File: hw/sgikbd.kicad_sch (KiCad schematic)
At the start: 16 parts, among them CON1 ISP, J1 SERIAL, SW1 RESET, SW2 SW_DPDT_x2, U1 ATMEGA88-20PU, U2 intkbd, U3 ps2conn, U4 kbout, Y1 Crystal

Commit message: schematic progress
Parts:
- removed CON1: ISP, AVR-ISP-6, symbol sgikbd-rescue:AVR-ISP-6
- removed J1: SERIAL, symbol sgikbd-rescue:CONN_01X04
- removed R2, R3: 4.7k, symbol sgikbd-rescue:R
- removed SW2: SW_DPDT_x2, symbol sgikbd-rescue:SW_DPDT_x2
- removed U1: ATMEGA88-20PU, DIL28, symbol sgikbd-rescue:ATMEGA88-20PU
- removed U2: intkbd, symbol sgikbd-rescue:sgikbd_conn
- removed U3: ps2conn, symbol sgikbd-rescue:ps2conn
- removed U4: kbout, symbol sgikbd-rescue:sgikbd_conn
- added C? (x4): 0.33uF, symbol Device:C_Polarized
- added J?: AVR-ISP, symbol Connector:AVR-ISP-6
- added R? (x2): 4.7k, symbol sgikbd-rescue:R
- added U?: sgi-db15, Connector_Dsub:DSUB-15_Female_Horizontal_P2.77x2.84mm_EdgePinOffset7.70mm_Housed_MountingHolesOffset9.12mm, symbol sgikbd:sgi-db15
- added U? (x3): LM358, symbol Amplifier_Operational:LM358
- added U?: ps2kbd, symbol sgikbd:ps2conn
- added U?: sgi-db9, Connector_Dsub:DSUB-9_Female_Horizontal_P2.77x2.84mm_EdgePinOffset7.70mm_Housed_MountingHolesOffset9.12mm, symbol sgikbd:sgi-db9
- added U?: L7805, symbol Regulator_Linear:L7805
- added U?: L7905, symbol Regulator_Linear:L7905
- added U?: ps2mouse, symbol sgikbd:ps2conn
- added U?: ATmega328PB-A, Package_QFP:TQFP-32_7x7mm_P0.8mm, symbol MCU_Microchip_ATmega:ATmega328PB-A
- added U?: sgi-mdin6, symbol sgikbd:sgi-mdin6
- Y1: value Crystal -> 14.7456MHz
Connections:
- net GND: now also C3.1, C4.1, C?.1, C?.1, C?.2, C?.2, J?.6 (GND), R?.2, U?.1 (GND), U?.1 (GND), U?.2 (GND), U?.2 (GND), U?.21 (GND), U?.3 (GND), U?.3 (GND), U?.3 (GND), U?.3 (GND), U?.5 (GND), U?.6 (GND), U?.9 (GND); no longer C3.2, C4.2
- net SCK: now also J?.3 (SCK), U?.17 (PB5)
- net VCC: now also C?.1, J?.2 (VCC), R?.1, U?.18 (AVCC), U?.3 (OUT), U?.4 (VCC), U?.4 (VCC), U?.4 (VCC), U?.8 (V+)
- net XTAL0: now also C4.2, U?.7 (XTAL1/PB6); no longer C4.1
- net XTAL1: now also C3.2, U?.8 (XTAL2/PB7); no longer C3.1
- net ~{RESET}: now also J?.5 (~{RST}), U?.29 (~{RESET}/PC6)
- new net: U?.10 (MRXD), U?.2 (MRXD), U?.5 (MRXD), U?.7
- new net: U?.11 (NC), U?.12 (NC)
- new net: U?.4 (KBTXD), U?.5 (KBTXD), U?.8 (KBTXD)
- new net: U?.1, U?.1 (KBRX), U?.2 (KBRXD), U?.5 (KBRXD)
- new net: R?.1, R?.2, U?.2 (-), U?.6 (-)
- new net: U?.1 (NC), U?.3 (NC)
- new net +12V: C?.1, U?.1 (IN), U?.4 (+8V), U?.7 (+12V), U?.7 (+12V), U?.8 (+12V), U?.9 (+12V)
- new net -5V: C?.2, U?.3 (VO), U?.4 (V-)
- new net KBCLK: U?.32 (PD2), U?.5 (CLK)
- new net KBDATA: U?.1 (DATA), U?.2 (PD4)
- new net MCLK: U?.1 (PD3), U?.5 (CLK)
- new net MDATA: U?.1 (DATA), U?.9 (PD5)
- new net RXD0: U?.30 (PD0)
- new net RXD1_MISO: J?.1 (MISO), U?.16 (PB4)
- new net TXD0: U?.3 (+), U?.31 (PD1)
- new net TXD1_MOSI: J?.4 (MOSI), U?.15 (PB3), U?.5 (+)
- new net VBUS-: C?.2, U?.15 (-12V), U?.2 (VI), U?.4 (-12V), U?.6 (-8V)
- no-connect marks 10 -> 16
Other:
- moved on the sheet: C3, C4, R1, SW1, Y1

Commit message: first board revision completed
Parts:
- removed C1, C2: 0.1uF, symbol sgikbd-rescue:C
- removed C3, C4: 22pF, symbol sgikbd-rescue:C
- removed C?: 0.33uF, symbol Device:C_Polarized
- removed R1, R? (x2): 4.7k, symbol sgikbd-rescue:R
- removed SW1: RESET, symbol sgikbd-rescue:SW_Push
- removed Y1: 14.7456MHz, symbol sgikbd-rescue:Crystal
- added C1, C2: 22pF, Capacitor_SMD:C_0805_2012Metric_Pad1.18x1.45mm_HandSolder, symbol Device:C
- added C3, C6, C7, C9: 0.1uF, Capacitor_SMD:C_0805_2012Metric_Pad1.18x1.45mm_HandSolder, symbol Device:C
- added D1: 1N4148, Diode_SMD:D_SOD-123, symbol Diode:1N4148W
- added H1, H2, H3, H4: mounting hole, MountingHole:MountingHole_3.2mm_M3_Pad, symbol Mechanical:MountingHole_Pad
- added R1, R2, R3, R4: 4.7k, Resistor_SMD:R_0805_2012Metric_Pad1.20x1.40mm_HandSolder, symbol Device:R
- added SW1: RESET, Button_Switch_SMD:SW_Push_1P1T_NO_6x6mm_H9.5mm, symbol Switch:SW_Push
- added Y1: 3.6864MHz, Crystal:Crystal_SMD_HC49-SD, symbol Device:Crystal
- C4, C5, C8: renamed from C?; footprint (none) -> Capacitor_SMD:CP_Elec_4x5.4
- J1: renamed from J?; footprint (none) -> Connector_IDC:IDC-Header_2x03_P2.54mm_Vertical
- U1: renamed from U?; value ATmega328PB-A -> ATmega328PB
- U2, U5: renamed from U?; footprint (none) -> sgikbd:minidin6
- U3: renamed from U?; value ps2mouse -> ps2aux; footprint (none) -> sgikbd:minidin6
- U4: renamed from U?; footprint (none) -> Package_SO:SOIC-8_3.9x4.9mm_P1.27mm
- U6: renamed from U?; footprint (none) -> Package_TO_SOT_SMD:TO-252-3_TabPin2
- U7: renamed from U?; footprint (none) -> Package_TO_SOT_SMD:SOT-89-3_Handsoldering
- gave numbers to parts that had none: 2
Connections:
- net -5V: now also C9.2
- net GND: now also U2.0 (shield), U3.0 (shield), U5.0 (shield), U8.0 (shield), U9.0 (shield), C1.2, C2.2, C3.2, C6.2, C7.2, C9.1, H1.1, H2.1, H3.1, H4.1, R3.2, R4.2, SW1.2
- net RXD0: now also D1.1 (K), R4.1
- net VCC: now also C3.1, C6.1, C7.1, R1.1, R2.1
- net XTAL0: now also C1.1, Y1.2
- net XTAL1: now also C2.1, Y1.1
- net ~{RESET}: now also R1.2, SW1.1
- net SGIMRX: now reaches U4.7, U5.2 (MRXD), U8.5 (MRXD), U9.10 (MRXD)
- net at U9.11 (NC): no longer U9.12 (NC)
- net SGIKBTX: now reaches U5.5 (KBTXD), U8.8 (KBTXD), U9.4 (KBTXD)
- net SGIKBTX: now also D1.2 (A)
- net SGIKBRX: now reaches U4.1, U5.1 (KBRX), U8.2 (KBRXD), U9.5 (KBRXD)
- net VREF: now reaches U4.2 (-), U4.6 (-)
- net VREF: now also R2.2, R3.1
- net at U8.1 (NC): no longer U8.3 (NC)
- net +12V renamed VBUS+
- net RXD1_MISO renamed MISO
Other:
- moved on the sheet: C4, C5, C8, J1, U1, U4A, U4B, U6, U7

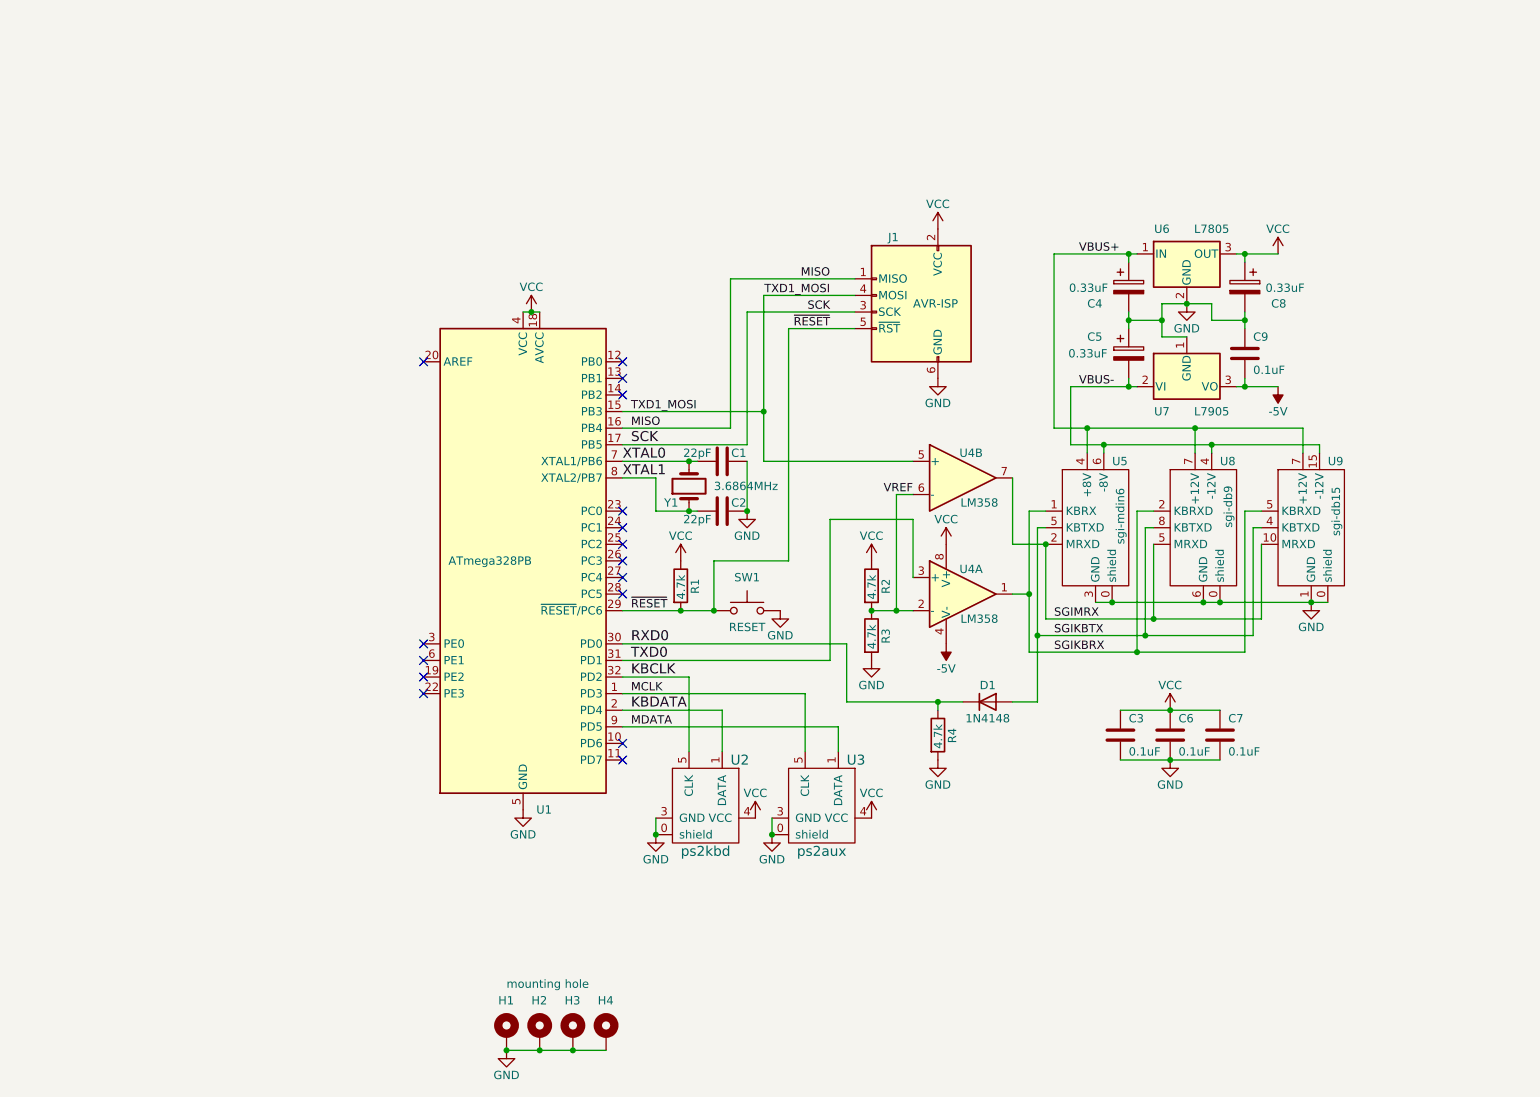
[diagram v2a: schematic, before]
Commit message: fixed UART polarity
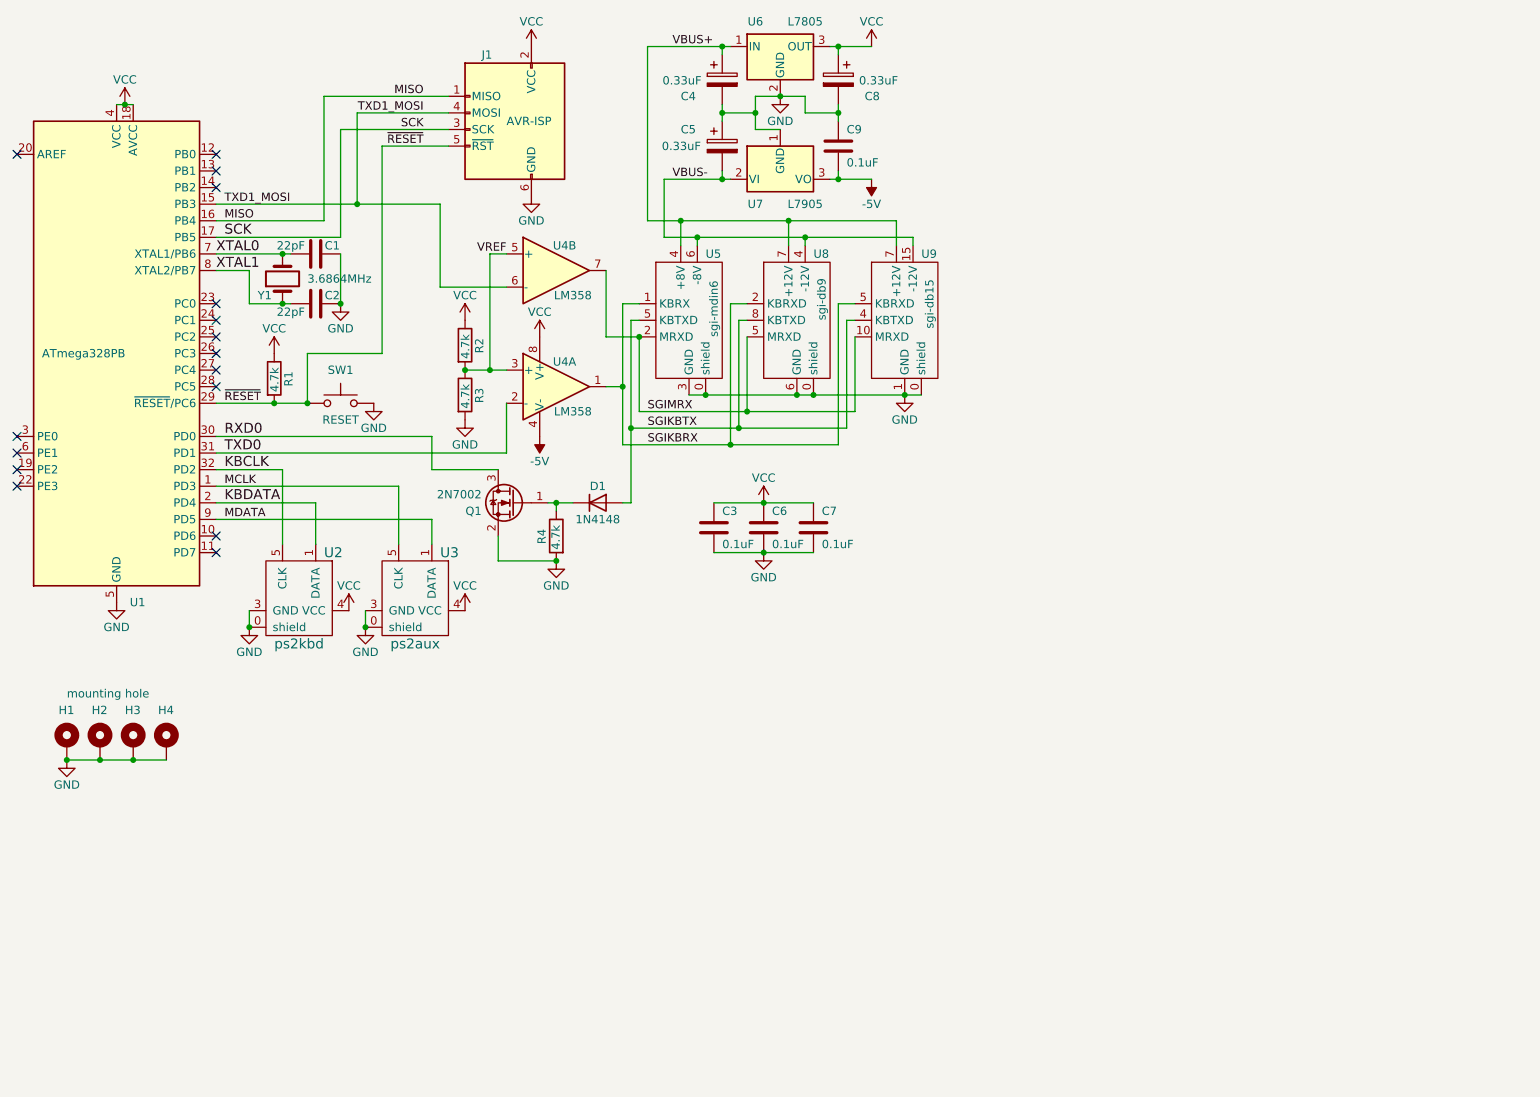
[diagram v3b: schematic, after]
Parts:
- added Q1: 2N7002, Package_TO_SOT_SMD:SOT-23, symbol Transistor_FET:2N7002
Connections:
- net GND: now also Q1.2 (S)
- net RXD0: now also Q1.3 (D); no longer D1.1 (K), R4.1
- net TXD0: now also U4.2 (-); no longer U4.3 (+)
- net TXD1_MOSI: now also U4.6 (-); no longer U4.5 (+)
- net VREF: now also U4.3 (+), U4.5 (+); no longer U4.2 (-), U4.6 (-)
- new net: D1.1 (K), Q1.1 (G), R4.1
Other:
- moved on the sheet: C1, C2, C3, C4, C5, C6, C7, C8, C9, D1, H1, H2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
